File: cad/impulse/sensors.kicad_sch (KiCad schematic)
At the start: 17 parts, among them SW101 SW_Push, U10 BMI270, U9 HP203B

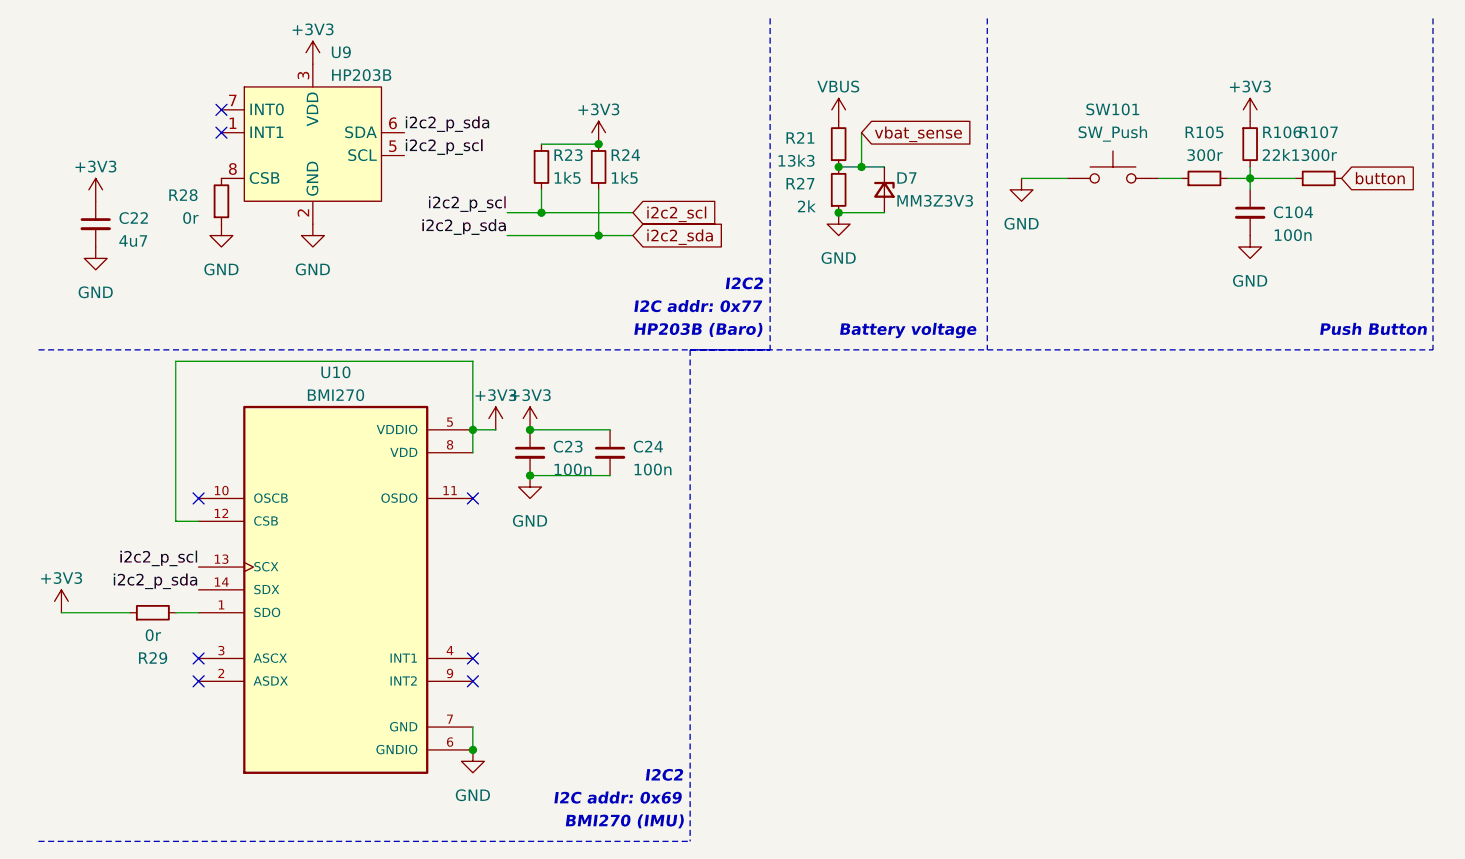
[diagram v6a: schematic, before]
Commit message: Modified oscillator circuit.
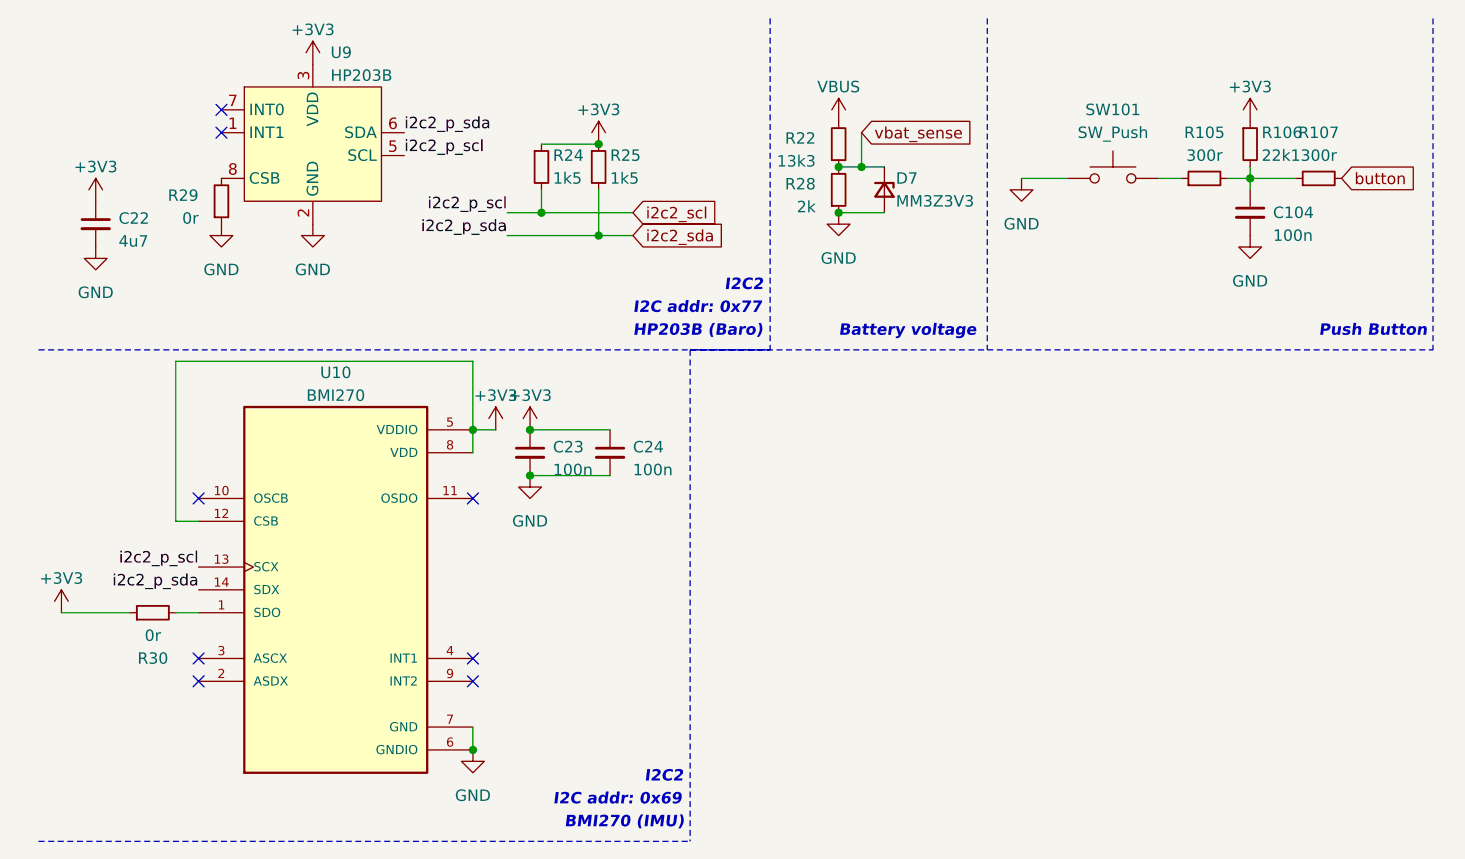
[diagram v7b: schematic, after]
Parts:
- renumbered R21 to R22, R23 to R24, R24 to R25, R27 to R28, R28 to R29, R29 to R30
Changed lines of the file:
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@@
   (symbol (lib_id "Device:R_Small") (at 74.93 29.21 0) (unit 1)
     (in_bom yes) (on_board yes) (dnp no)
-    (property "Reference" "R24" (at 76.2 27.94 0)
+    (property "Reference" "R25" (at 76.2 27.94 0)
       (effects (font (size 1.27 1.27)) (justify left))
     )
@@
       (project "impulse"
         (path "/eb4cfece-5fcb-437a-ac58-337ab6512039/3cb4dd3b-38f5-4fc2-a791-3f5e2e74c848"
-          (reference "R24") (unit 1)
+          (reference "R25") (unit 1)
         )
       )
@@
   (symbol (lib_id "Device:R_Small") (at 25.4 78.74 90) (unit 1)
     (in_bom yes) (on_board yes) (dnp no)
-    (property "Reference" "R29" (at 25.4 83.82 90)
+    (property "Reference" "R30" (at 25.4 83.82 90)
       (effects (font (size 1.27 1.27)))
     )
@@
       (project "impulse"
         (path "/eb4cfece-5fcb-437a-ac58-337ab6512039/3cb4dd3b-38f5-4fc2-a791-3f5e2e74c848"
-          (reference "R29") (unit 1)
+          (reference "R30") (unit 1)
         )
       )
@@
   (symbol (lib_id "Device:R_Small") (at 101.6 26.67 0) (mirror x) (unit 1)
     (in_bom yes) (on_board yes) (dnp no) (fields_autoplaced)
-    (property "Reference" "R21" (at 99.06 26.035 0)
+    (property "Reference" "R22" (at 99.06 26.035 0)
       (effects (font (size 1.27 1.27)) (justify right))
     )
@@
       (project "impulse"
         (path "/eb4cfece-5fcb-437a-ac58-337ab6512039/3cb4dd3b-38f5-4fc2-a791-3f5e2e74c848"
-          (reference "R21") (unit 1)
+          (reference "R22") (unit 1)
         )
       )
@@
   (symbol (lib_id "Device:R_Small") (at 101.6 31.75 0) (mirror x) (unit 1)
     (in_bom yes) (on_board yes) (dnp no) (fields_autoplaced)
-    (property "Reference" "R27" (at 99.06 31.115 0)
+    (property "Reference" "R28" (at 99.06 31.115 0)
       (effects (font (size 1.27 1.27)) (justify right))
     )
@@
       (project "impulse"
         (path "/eb4cfece-5fcb-437a-ac58-337ab6512039/3cb4dd3b-38f5-4fc2-a791-3f5e2e74c848"
-          (reference "R27") (unit 1)
+          (reference "R28") (unit 1)
         )
       )
@@
       (project "impulse"
         (path "/eb4cfece-5fcb-437a-ac58-337ab6512039/3cb4dd3b-38f5-4fc2-a791-3f5e2e74c848"
-          (reference "R22") (unit 1)
+          (reference "R23") (unit 1)
         )
       )
@@
       (project "impulse"
         (path "/eb4cfece-5fcb-437a-ac58-337ab6512039/3cb4dd3b-38f5-4fc2-a791-3f5e2e74c848"
-          (reference "R26") (unit 1)
+          (reference "R27") (unit 1)
         )
       )
@@
   (symbol (lib_id "Device:R_Small") (at 33.02 33.02 0) (mirror x) (unit 1)
     (in_bom yes) (on_board yes) (dnp no) (fields_autoplaced)
-    (property "Reference" "R28" (at 30.48 32.385 0)
+    (property "Reference" "R29" (at 30.48 32.385 0)
       (effects (font (size 1.27 1.27)) (justify right))
     )
@@
       (project "impulse"
         (path "/eb4cfece-5fcb-437a-ac58-337ab6512039/3cb4dd3b-38f5-4fc2-a791-3f5e2e74c848"
-          (reference "R28") (unit 1)
+          (reference "R29") (unit 1)
         )
       )
@@
       (project "impulse"
         (path "/eb4cfece-5fcb-437a-ac58-337ab6512039/3cb4dd3b-38f5-4fc2-a791-3f5e2e74c848"
-          (reference "R25") (unit 1)
+          (reference "R26") (unit 1)
         )
       )
@@
   (symbol (lib_id "Device:R_Small") (at 68.58 29.21 0) (unit 1)
     (in_bom yes) (on_board yes) (dnp no)
-    (property "Reference" "R23" (at 69.85 27.94 0)
+    (property "Reference" "R24" (at 69.85 27.94 0)
       (effects (font (size 1.27 1.27)) (justify left))
     )
@@
       (project "impulse"
         (path "/eb4cfece-5fcb-437a-ac58-337ab6512039/3cb4dd3b-38f5-4fc2-a791-3f5e2e74c848"
-          (reference "R23") (unit 1)
-        )
-      )
+          (reference "R24") (unit 1)
+        )
+      )

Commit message: First layout.
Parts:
- renumbered R22 to R23, R24 to R25, R25 to R26, R28 to R29, R29 to R30, R30 to R31
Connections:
- net VBUS renamed vsense
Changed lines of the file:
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@@
+    (stroke (width 0) (type default))
+  )
+  (wire (pts (xy 101.6 20.32) (xy 101.6 24.13))
     (stroke (width 0) (type default))
   )
@@
     )
   )
+  (global_label "vsense" (shape input) (at 101.6 20.32 0) (fields_autoplaced)
+    (effects (font (size 1.27 1.27)) (justify left))
+    (property "Intersheetrefs" "${INTERSHEET_REFS}" (at 110.8558 20.32 0)
+      (effects (font (size 1.27 1.27)) (justify left) hide)
+    )
+  )
   (symbol (lib_id "power:+3V3") (at 15.24 78.74 0) (unit 1)
     (in_bom yes) (on_board yes) (dnp no) (fields_autoplaced)
@@
   (symbol (lib_id "Device:R_Small") (at 74.93 29.21 0) (unit 1)
     (in_bom yes) (on_board yes) (dnp no)
-    (property "Reference" "R25" (at 76.2 27.94 0)
+    (property "Reference" "R26" (at 76.2 27.94 0)
       (effects (font (size 1.27 1.27)) (justify left))
     )
@@
       (project "impulse"
         (path "/eb4cfece-5fcb-437a-ac58-337ab6512039/3cb4dd3b-38f5-4fc2-a791-3f5e2e74c848"
-          (reference "R25") (unit 1)
+          (reference "R26") (unit 1)
         )
       )
@@
   (symbol (lib_id "Device:R_Small") (at 25.4 78.74 90) (unit 1)
     (in_bom yes) (on_board yes) (dnp no)
-    (property "Reference" "R30" (at 25.4 83.82 90)
+    (property "Reference" "R31" (at 25.4 83.82 90)
       (effects (font (size 1.27 1.27)))
     )
@@
       (project "impulse"
         (path "/eb4cfece-5fcb-437a-ac58-337ab6512039/3cb4dd3b-38f5-4fc2-a791-3f5e2e74c848"
-          (reference "R30") (unit 1)
+          (reference "R31") (unit 1)
         )
       )
@@
   (symbol (lib_id "Device:R_Small") (at 101.6 26.67 0) (mirror x) (unit 1)
     (in_bom yes) (on_board yes) (dnp no) (fields_autoplaced)
-    (property "Reference" "R22" (at 99.06 26.035 0)
+    (property "Reference" "R23" (at 99.06 26.035 0)
       (effects (font (size 1.27 1.27)) (justify right))
     )
@@
       (project "impulse"
         (path "/eb4cfece-5fcb-437a-ac58-337ab6512039/3cb4dd3b-38f5-4fc2-a791-3f5e2e74c848"
-          (reference "R22") (unit 1)
+          (reference "R23") (unit 1)
         )
       )
@@
   (symbol (lib_id "Device:R_Small") (at 101.6 31.75 0) (mirror x) (unit 1)
     (in_bom yes) (on_board yes) (dnp no) (fields_autoplaced)
-    (property "Reference" "R28" (at 99.06 31.115 0)
+    (property "Reference" "R29" (at 99.06 31.115 0)
       (effects (font (size 1.27 1.27)) (justify right))
     )
@@
       (project "impulse"
         (path "/eb4cfece-5fcb-437a-ac58-337ab6512039/3cb4dd3b-38f5-4fc2-a791-3f5e2e74c848"
-          (reference "R28") (unit 1)
+          (reference "R29") (unit 1)
         )
       )
@@
       (project "impulse"
         (path "/eb4cfece-5fcb-437a-ac58-337ab6512039/3cb4dd3b-38f5-4fc2-a791-3f5e2e74c848"
-          (reference "R23") (unit 1)
+          (reference "R24") (unit 1)
         )
       )
@@
       (project "impulse"
         (path "/eb4cfece-5fcb-437a-ac58-337ab6512039/3cb4dd3b-38f5-4fc2-a791-3f5e2e74c848"
-          (reference "R27") (unit 1)
+          (reference "R28") (unit 1)
         )
       )
@@
   (symbol (lib_id "Device:R_Small") (at 33.02 33.02 0) (mirror x) (unit 1)
     (in_bom yes) (on_board yes) (dnp no) (fields_autoplaced)
-    (property "Reference" "R29" (at 30.48 32.385 0)
+    (property "Reference" "R30" (at 30.48 32.385 0)
       (effects (font (size 1.27 1.27)) (justify right))
     )
@@
       (project "impulse"
         (path "/eb4cfece-5fcb-437a-ac58-337ab6512039/3cb4dd3b-38f5-4fc2-a791-3f5e2e74c848"
-          (reference "R29") (unit 1)
+          (reference "R30") (unit 1)
         )
       )
@@
       (project "impulse"
         (path "/eb4cfece-5fcb-437a-ac58-337ab6512039/3cb4dd3b-38f5-4fc2-a791-3f5e2e74c848"
-          (reference "R26") (unit 1)
+          (reference "R27") (unit 1)
         )
       )
@@
   (symbol (lib_id "Device:R_Small") (at 68.58 29.21 0) (unit 1)
     (in_bom yes) (on_board yes) (dnp no)
-    (property "Reference" "R24" (at 69.85 27.94 0)
+    (property "Reference" "R25" (at 69.85 27.94 0)
       (effects (font (size 1.27 1.27)) (justify left))
     )
@@
       (project "impulse"
         (path "/eb4cfece-5fcb-437a-ac58-337ab6512039/3cb4dd3b-38f5-4fc2-a791-3f5e2e74c848"
-          (reference "R24") (unit 1)
+          (reference "R25") (unit 1)
         )
       )
@@
         )
       )
-    )
-  )
-  (symbol (lib_id "power:VBUS") (at 101.6 24.13 0) (unit 1)
-    (in_bom yes) (on_board yes) (dnp no) (fields_autoplaced)
-    (property "Reference" "#PWR058" (at 101.6 27.94 0)
-      (effects (font (size 1.27 1.27)) hide)
-    )
-    (property "Value" "VBUS" (at 101.6 20.32 0)
-      (effects (font (size 1.27 1.27)))
-    )
-    (property "Footprint" "" (at 101.6 24.13 0)
-      (effects (font (size 1.27 1.27)) hide)
-    )
-    (property "Datasheet" "" (at 101.6 24.13 0)
-      (effects (font (size 1.27 1.27)) hide)
-    )
-    (pin "1")
-    (instances
-      (project "impulse"
-        (path "/eb4cfece-5fcb-437a-ac58-337ab6512039/3cb4dd3b-38f5-4fc2-a791-3f5e2e74c848"
-          (reference "#PWR058") (unit 1)
-        )
-      )
